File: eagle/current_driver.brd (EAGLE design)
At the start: 100.3 x 80 mm, 46 parts, among them IC4 UA78M05DCY, J1 Hall_Stop, J10 S5, J11 S1, J12 S2, J2 SIG_TEST, J3 S3, J9 S4, K2 4052, Q1 60V/32A/35mΩ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

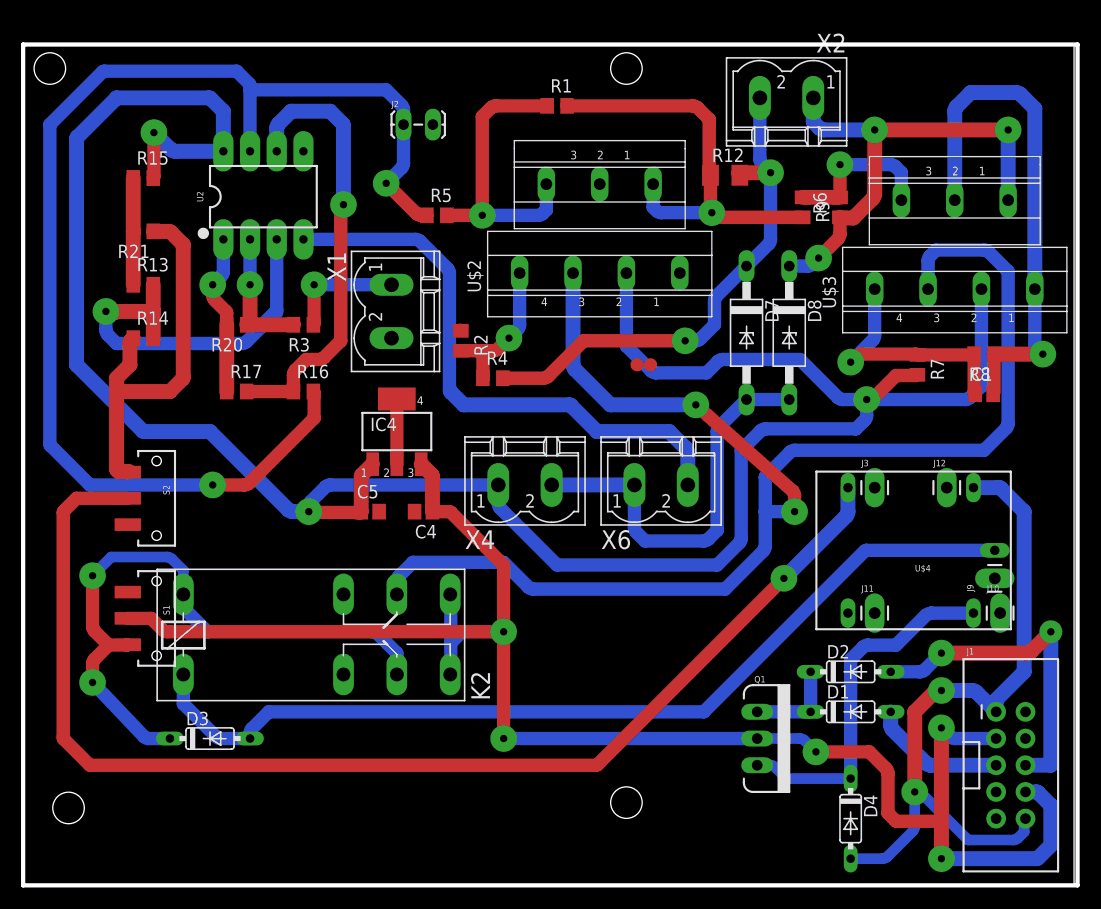
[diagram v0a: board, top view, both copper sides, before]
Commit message: modified Rs current sense resistor footprint
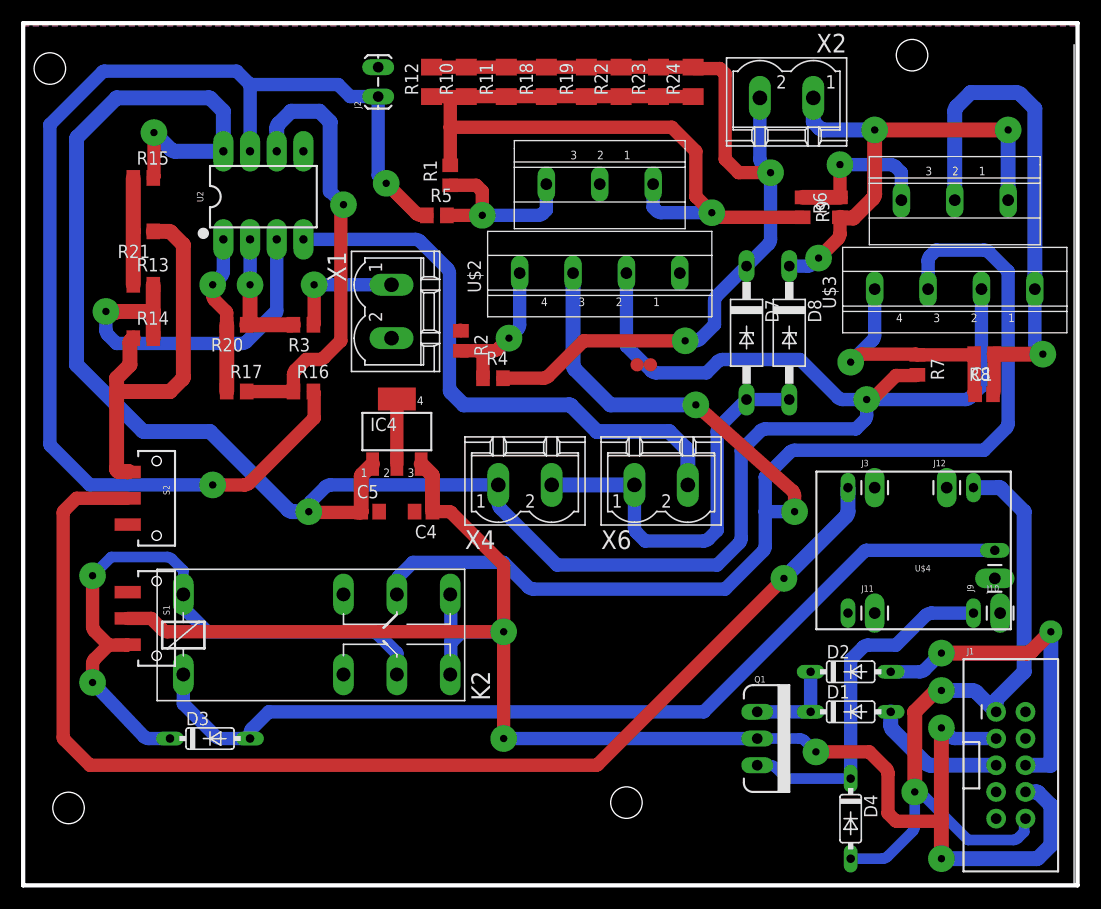
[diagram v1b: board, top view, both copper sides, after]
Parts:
- added R10, R11, R18, R19, R22, R23, R24: .301, rcl:M1206
- moved R12 29.3 mm to (38.9, 76.5), turned to 90 degrees
- moved R1 12.1 mm to (40.6, 67.6), turned to 90 degrees
- moved J2 3.78 mm to (33.8, 75.2), turned to 90 degrees
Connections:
- removed net N$1: R1.2, R12.1, R9.2, U$2.6
- new net N$19: R1.2, R10.1, R11.1, R12.1, R18.1, R19.1, R22.1, R23.1, R24.1, R9.2, U$2.6
- net N$3: now also R10.2, R11.2, R18.2, R19.2, R22.2, R23.2, R24.2
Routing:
- net N$19: track 0.00 -> 79.0 mm, vias 0 -> 1
- net N$1: track 39.7 -> 0.00 mm, vias 1 -> 0
- net N$3: track 49.6 -> 87.4 mm
- net N$2: track 28.0 -> 17.7 mm
- net VIN: track 118.6 -> 116.8 mm
- net N$17: track 42.4 -> 41.8 mm
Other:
- board size 100.3 x 80 mm -> 100.3 x 82 mm
